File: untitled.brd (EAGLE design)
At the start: 59.4 x 57.8 mm, 24 parts

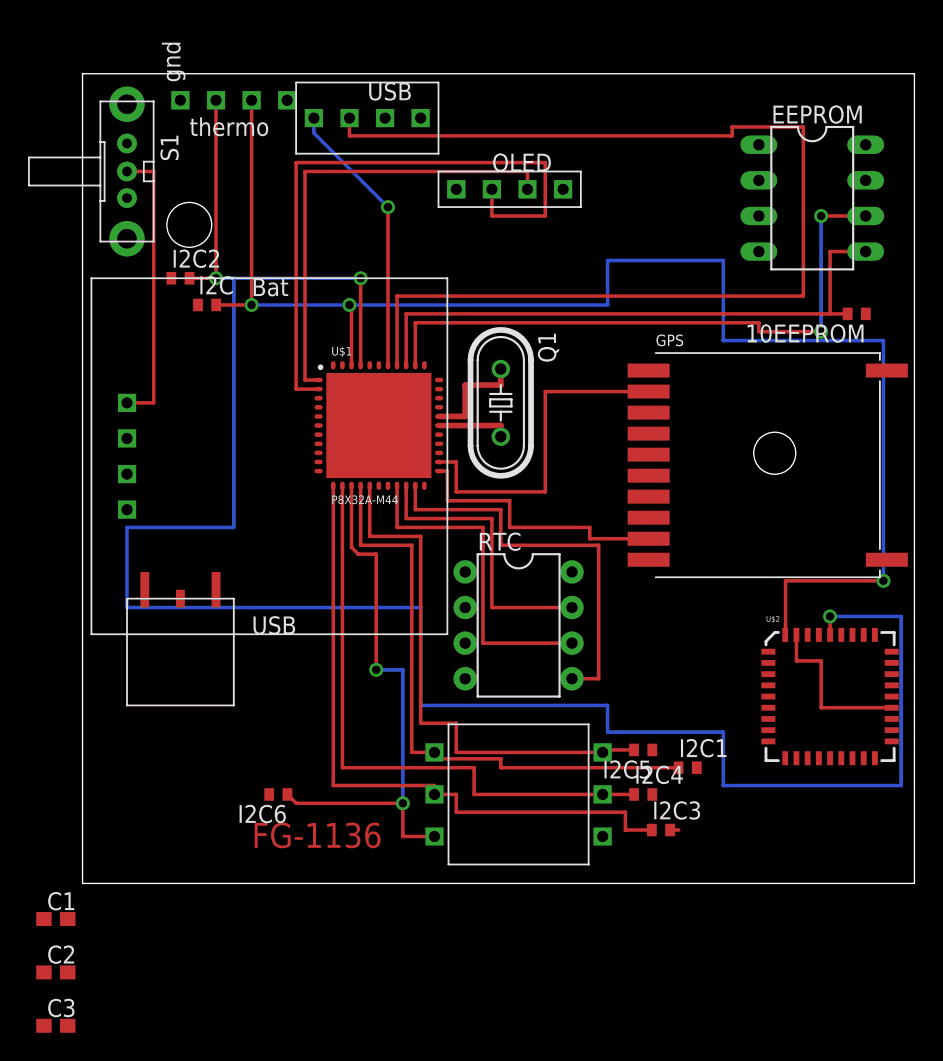
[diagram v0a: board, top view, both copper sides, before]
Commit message: Routed some power and decoupling caps
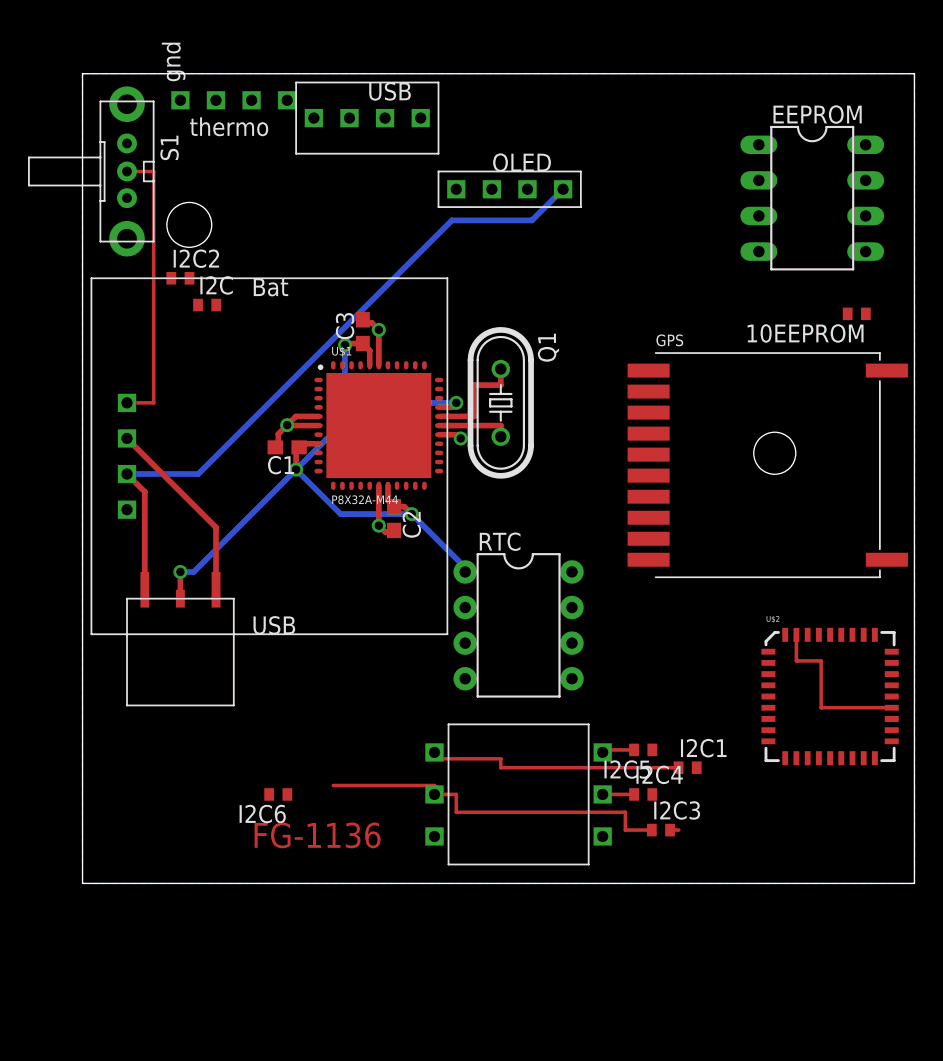
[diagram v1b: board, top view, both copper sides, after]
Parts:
- moved C3 54.2 mm to (53.7, 49.5), turned to 90 degrees
- moved C2 40.4 mm to (55.9, 36.2), turned to 270 degrees
- moved C1 37.5 mm to (48.3, 41.3), turned to 180 degrees
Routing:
- net SCL: track 148.6 -> 0.00 mm, vias 3 -> 0
- net SDA: track 103.5 -> 0.00 mm, vias 3 -> 0
- net N$9: track 80.3 -> 0.00 mm
- net +3V3: track 0.00 -> 57.4 mm, vias 0 -> 5
- net +5V: track 0.00 -> 47.7 mm
- net N$10: track 45.1 -> 0.00 mm
- net N$19: track 44.1 -> 0.00 mm, vias 2 -> 0
- net N$18: track 42.2 -> 0.00 mm
- net N$20: track 42.8 -> 2.24 mm
- net N$15: track 39.2 -> 0.00 mm, vias 2 -> 0
- net N$21: track 38.1 -> 2.42 mm
- net N$11: track 33.0 -> 0.00 mm
- net GND: track 0.00 -> 29.3 mm, vias 0 -> 4
- net N$5: track 28.8 -> 0.00 mm
- net N$14: track 42.8 -> 18.5 mm
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- added copper zone on layer 16, net GND

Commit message: Finished PCB V2
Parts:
- added C4: (no value), SparkFun:0603
- moved 10EEPROM 14.0 mm to (74.9, 49.8), turned to 0 degrees
- moved I2C2 8.25 mm to (43.8, 61.0)
- moved I2C 4.72 mm to (46.0, 54.6)
- moved I2C6 3.93 mm to (51.4, 15.6)
- moved I2C1 2.86 mm to (79.7, 18.4)
- moved C2 2.56 mm to (56.2, 33.7)
- moved C3 1.59 mm to (53.7, 51.1)
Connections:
- net +3V3: now also C4.1, GPS.P$1, GPS.P$4
- net GND: now also C4.2, GPS.P$3
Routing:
- net +3V3: track 57.4 -> 281.9 mm, vias 5 -> 10
- net SCL: track 0.00 -> 104.5 mm, vias 0 -> 2
- net SDA: track 0.00 -> 95.4 mm, vias 0 -> 2
- net N$15: track 0.00 -> 80.5 mm
- net N$18: track 0.00 -> 67.8 mm
- net GND: track 29.3 -> 79.9 mm, vias 4 -> 6
- net N$20: track 2.24 -> 42.1 mm
- net N$19: track 0.00 -> 39.2 mm
- net N$8: track 0.00 -> 36.5 mm
- net N$21: track 2.42 -> 38.1 mm
- net N$6: track 0.00 -> 32.9 mm
- net N$11: track 0.00 -> 32.5 mm, vias 0 -> 1
- net N$10: track 0.00 -> 31.1 mm, vias 0 -> 1
- net N$14: track 18.5 -> 45.0 mm
- net N$5: track 0.00 -> 24.5 mm
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
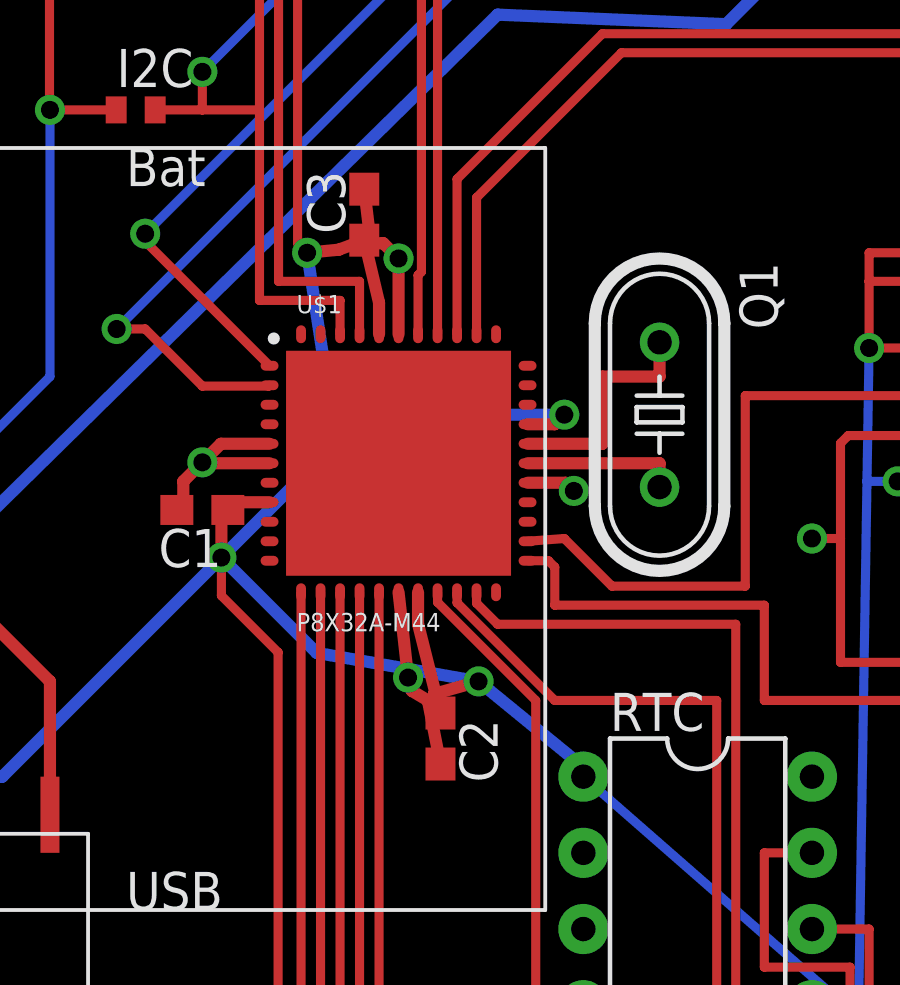
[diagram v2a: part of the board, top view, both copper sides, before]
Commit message: fixed shorted caps
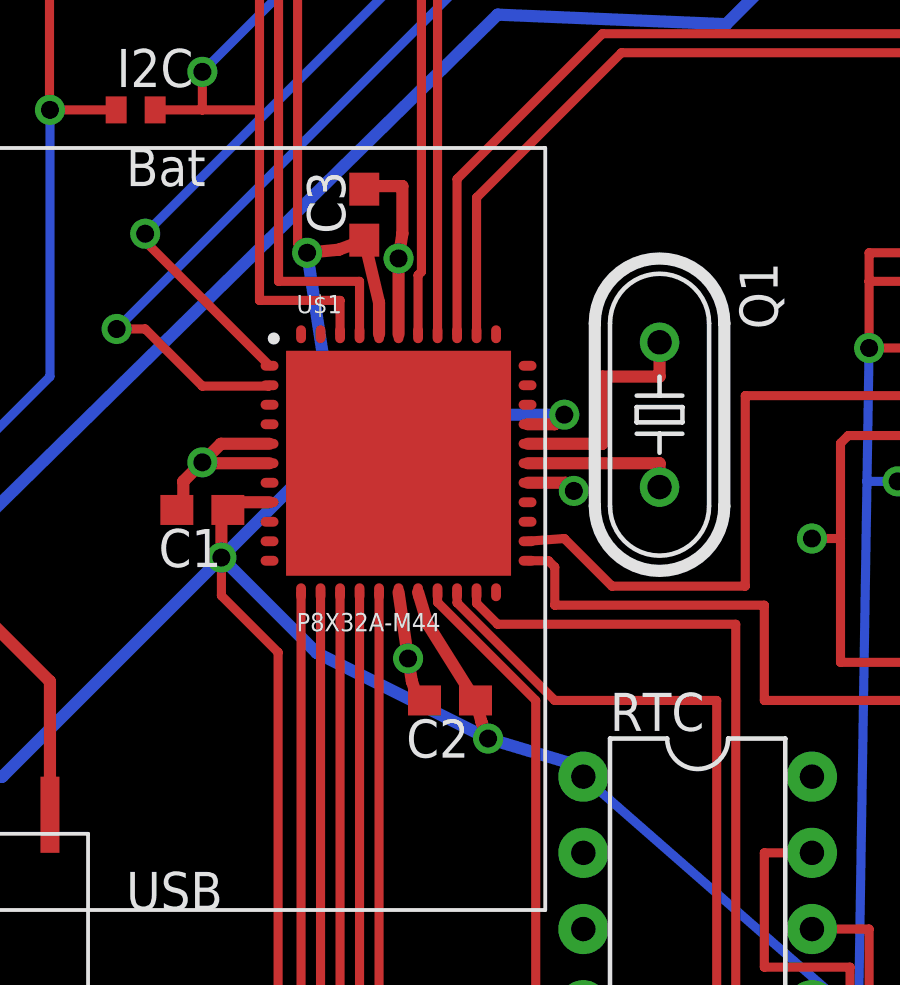
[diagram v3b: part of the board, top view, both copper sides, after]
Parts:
- moved C2 1.31 mm to (56.5, 34.9), turned to 180 degrees
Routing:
- net GND: track 79.9 -> 78.5 mm
- net +3V3: track 281.9 -> 280.7 mm
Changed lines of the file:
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@@
 <element name="U$2" library="SparkFun" package="LCC36" value="HMC6343A" x="86.995" y="23.495"/>
 <element name="C1" library="rcl" package="C0603" value="" x="48.26" y="41.275" rot="R180"/>
-<element name="C2" library="rcl" package="C0603" value="" x="56.1975" y="33.655" rot="R270"/>
+<element name="C2" library="rcl" package="C0603" value="" x="56.515" y="34.925" rot="R180"/>
 <element name="C3" library="rcl" package="C0603" value="" x="53.6575" y="51.1175" rot="R90"/>
 <element name="C4" library="SparkFun" package="0603" value="" x="79.6925" y="25.0825" rot="R90"/>
@@
 <vertex x="33.655" y="10.16"/>
 </polygon>
-<wire x1="54.8" y1="38.5313" x2="55.1175" y2="35.6875" width="0.4064" layer="1"/>
-<wire x1="55.245" y1="35.2425" x2="55.7775" y2="34.925" width="0.4064" layer="1"/>
-<wire x1="55.7775" y1="34.925" x2="56.1975" y2="32.805" width="0.4064" layer="1"/>
+<wire x1="54.8" y1="38.5313" x2="55.1175" y2="36.3225" width="0.4064" layer="1"/>
+<wire x1="55.245" y1="35.56" x2="55.46" y2="34.925" width="0.4064" layer="1"/>
+<wire x1="55.46" y1="34.925" x2="55.665" y2="34.925" width="0.4064" layer="1"/>
 <wire x1="54.8" y1="47.1313" x2="54.8" y2="49.6575" width="0.4064" layer="1"/>
-<wire x1="54.2925" y1="50.165" x2="53.8725" y2="50.165" width="0.4064" layer="1"/>
-<wire x1="53.8725" y1="50.165" x2="53.6575" y2="51.9675" width="0.4064" layer="1"/>
 <wire x1="50.5" y1="42.8313" x2="48.2288" y2="42.8313" width="0.4064" layer="1"/>
 <wire x1="48.2288" y1="42.8313" x2="47.625" y2="42.2275" width="0.4064" layer="1"/>
@@
 <via x="48.26" y="42.8625" extent="1-16" drill="0.6"/>
 <via x="54.8" y="49.6575" extent="1-16" drill="0.6"/>
-<wire x1="54.8" y1="49.6575" x2="54.2925" y2="50.165" width="0.4064" layer="1"/>
-<via x="55.1175" y="35.6875" extent="1-16" drill="0.6"/>
+<wire x1="54.8" y1="49.6575" x2="54.9275" y2="50.4825" width="0.4064" layer="1"/>
+<via x="55.1175" y="36.3225" extent="1-16" drill="0.6"/>
 <wire x1="59.1" y1="42.1813" x2="60.3712" y2="42.1813" width="0.4064" layer="1"/>
 <wire x1="60.3712" y1="42.1813" x2="60.6425" y2="41.91" width="0.4064" layer="1"/>
 <via x="60.6425" y="41.91" extent="1-16" drill="0.6"/>
-<wire x1="55.245" y1="35.2425" x2="55.1175" y2="35.6875" width="0.4064" layer="1"/>
+<wire x1="55.245" y1="35.56" x2="55.1175" y2="36.3225" width="0.4064" layer="1"/>
 <wire x1="43.18" y1="31.75" x2="43.18" y2="35.56" width="0.4064" layer="1"/>
 <wire x1="43.18" y1="35.56" x2="36.83" y2="41.91" width="0.4064" layer="1"/>
@@
 <via x="68.58" y="40.3225" extent="1-16" drill="0.6" shape="octagon"/>
 <wire x1="68.58" y1="40.3225" x2="69.5325" y2="40.3225" width="0.3048" layer="1"/>
+<wire x1="54.9275" y1="50.4825" x2="54.9275" y2="52.07" width="0.4064" layer="1"/>
+<wire x1="54.9275" y1="52.07" x2="53.6575" y2="52.07" width="0.4064" layer="1"/>
+<wire x1="53.6575" y1="52.07" x2="53.6575" y2="51.9675" width="0.4064" layer="1"/>
 </signal>
 <signal name="+5V">
@@
 <wire x1="50.5" y1="41.5313" x2="49.11" y2="41.5313" width="0.4064" layer="1"/>
 <wire x1="49.11" y1="41.5313" x2="49.11" y2="41.275" width="0.4064" layer="1"/>
-<wire x1="55.45" y1="38.5313" x2="55.45" y2="37.475" width="0.4064" layer="1"/>
+<wire x1="55.45" y1="38.5313" x2="55.7675" y2="37.475" width="0.4064" layer="1"/>
 <wire x1="54.15" y1="47.1313" x2="54.15" y2="48.1875" width="0.4064" layer="1"/>
 <wire x1="40.64" y1="30.48" x2="40.64" y2="32.385" width="0.4064" layer="1"/>
@@
 <wire x1="48.895" y1="39.6875" x2="48.895" y2="41.06" width="0.4064" layer="1"/>
 <wire x1="48.895" y1="41.06" x2="49.11" y2="41.275" width="0.4064" layer="1"/>
-<wire x1="56.1975" y1="34.505" x2="55.9825" y2="35.14" width="0.4064" layer="1"/>
-<wire x1="55.9825" y1="35.14" x2="57.4675" y2="35.56" width="0.4064" layer="1"/>
-<via x="57.4675" y="35.56" extent="1-16" drill="0.6"/>
-<wire x1="57.4675" y1="35.56" x2="52.07" y2="36.5125" width="0.4064" layer="16"/>
+<wire x1="57.365" y1="34.925" x2="57.57" y2="34.1875" width="0.4064" layer="1"/>
+<wire x1="57.57" y1="34.1875" x2="57.785" y2="33.655" width="0.4064" layer="1"/>
+<via x="57.785" y="33.655" extent="1-16" drill="0.6"/>
+<wire x1="57.785" y1="33.655" x2="52.07" y2="36.5125" width="0.4064" layer="16"/>
 <wire x1="52.07" y1="36.5125" x2="48.895" y2="39.6875" width="0.4064" layer="16"/>
 <wire x1="59.1" y1="44.1313" x2="60.0063" y2="44.1313" width="0.4064" layer="1"/>
@@
 <wire x1="52.3875" y1="45.72" x2="53.6575" y2="44.45" width="0.4064" layer="16"/>
 <wire x1="54.15" y1="48.1875" x2="53.6575" y2="50.2675" width="0.4064" layer="1"/>
-<wire x1="55.45" y1="37.475" x2="56.1975" y2="34.505" width="0.4064" layer="1"/>
+<wire x1="55.7675" y1="37.475" x2="57.365" y2="34.925" width="0.4064" layer="1"/>
 <wire x1="60.96" y1="32.385" x2="60.96" y2="32.7025" width="0.4064" layer="16"/>
-<wire x1="60.96" y1="32.7025" x2="57.4675" y2="35.56" width="0.4064" layer="16"/>
+<wire x1="60.96" y1="32.7025" x2="57.785" y2="33.655" width="0.4064" layer="16"/>
 <wire x1="60.96" y1="32.385" x2="70.130975" y2="24.360396875" width="0.3048" layer="16"/>
 <wire x1="70.130975" y1="24.360396875" x2="73.66" y2="21.2725" width="0.3048" layer="16"/>

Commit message: cleaned
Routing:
- net +3V3: track 280.7 -> 289.7 mm
- net SDA: track 95.4 -> 97.0 mm
- net GND: track 78.5 -> 80.1 mm
- net N$18: track 67.8 -> 69.1 mm
- net SCL: track 104.5 -> 103.3 mm
- net N$10: track 31.1 -> 32.2 mm
- net N$5: track 24.5 -> 24.0 mm
- net N$17: track 47.3 -> 46.8 mm
- net N$15: track 80.5 -> 81.0 mm

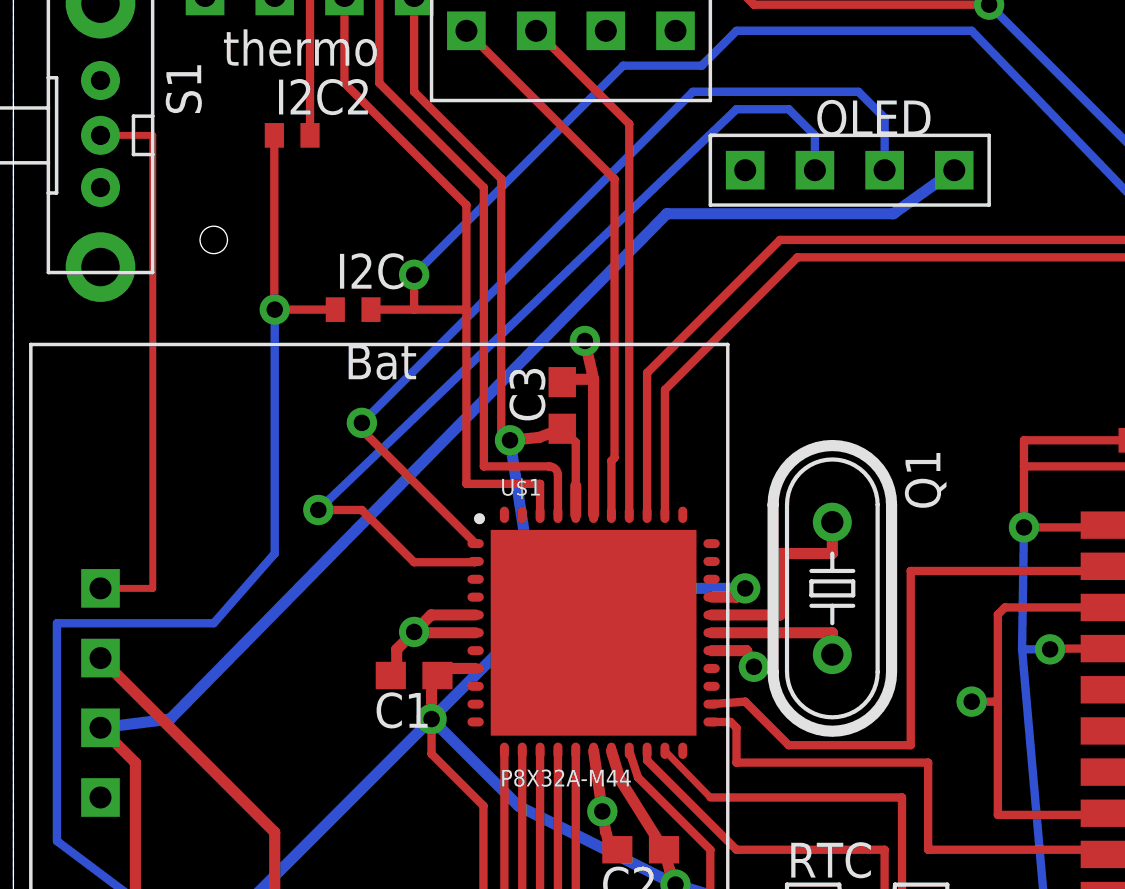
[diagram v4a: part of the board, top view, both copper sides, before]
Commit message: Reconnect GND to OLED header
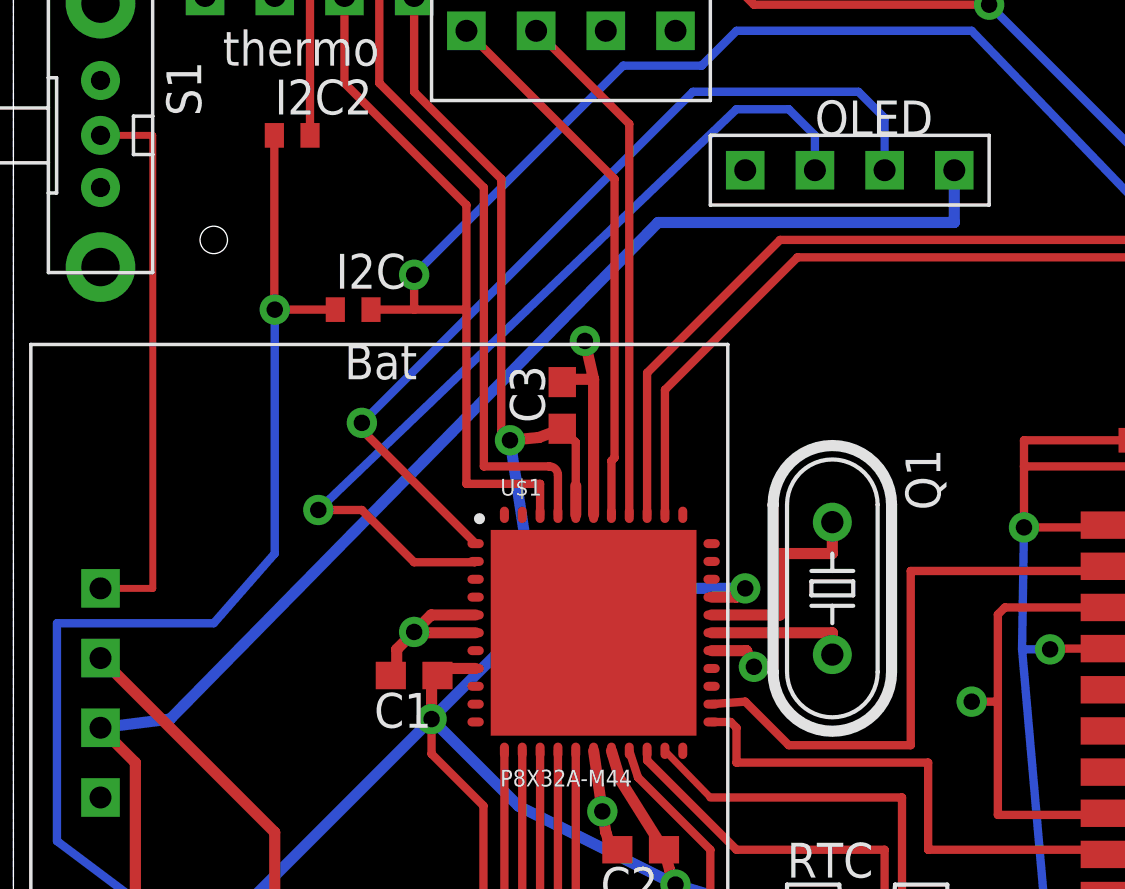
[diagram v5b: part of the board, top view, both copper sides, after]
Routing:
- net +5V: track 47.5 -> 48.8 mm
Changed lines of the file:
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@@
 <wire x1="53.6575" y1="52.07" x2="53.6575" y2="51.9675" width="0.4064" layer="1"/>
 <wire x1="53.6575" y1="52.07" x2="54.8" y2="52.07" width="0.4064" layer="1"/>
-<wire x1="60.325" y1="59.69" x2="57.785" y2="64.77" width="0" layer="19" extent="1-1"/>
 </signal>
 <signal name="+5V">
@@
 <wire x1="38.1" y1="38.1" x2="36.83" y2="39.37" width="0.4064" layer="1"/>
 <wire x1="36.83" y1="39.37" x2="39.37" y2="39.6875" width="0.4064" layer="16"/>
-<wire x1="39.37" y1="39.6875" x2="57.4675" y2="58.1025" width="0.4064" layer="16"/>
-<wire x1="57.4675" y1="58.1025" x2="65.7225" y2="58.1025" width="0.4064" layer="16"/>
-<wire x1="65.7225" y1="58.1025" x2="67.945" y2="59.69" width="0.4064" layer="16"/>
+<wire x1="39.37" y1="39.6875" x2="57.15" y2="57.785" width="0.4064" layer="16"/>
+<wire x1="57.15" y1="57.785" x2="67.945" y2="57.785" width="0.4064" layer="16"/>
+<wire x1="67.945" y1="57.785" x2="67.945" y2="59.69" width="0.4064" layer="16"/>
 </signal>
 <signal name="+3V3">
